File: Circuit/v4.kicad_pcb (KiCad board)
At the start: 2 copper layers, 40 x 49.4 mm, 41 parts, among them J1 Battery, J2 AVR-ISP-6, J3 TX Connector, J4 RX Connector, J5 Alt Battery, J6 Alt RX Conn, J7 Alt TX Conn, J8 Remote temp input 47K @ 25oC, Q1 IRLML6244TRPBF, U1 EL3H7(B)(TA)-VG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

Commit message: Change Opto to HMHA2801
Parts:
- U1: value EL3H7(B)(TA)-VG -> HMHA2801
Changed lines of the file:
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@@
       (effects (font (size 1 1) (thickness 0.15)))
     )
-    (fp_text value "EL3H7(B)(TA)-VG" (at 0.1524 -3.302 180) (layer F.Fab)
+    (fp_text value HMHA2801 (at 0.1524 -3.302 180) (layer F.Fab)
       (effects (font (size 1 1) (thickness 0.15)))
     )

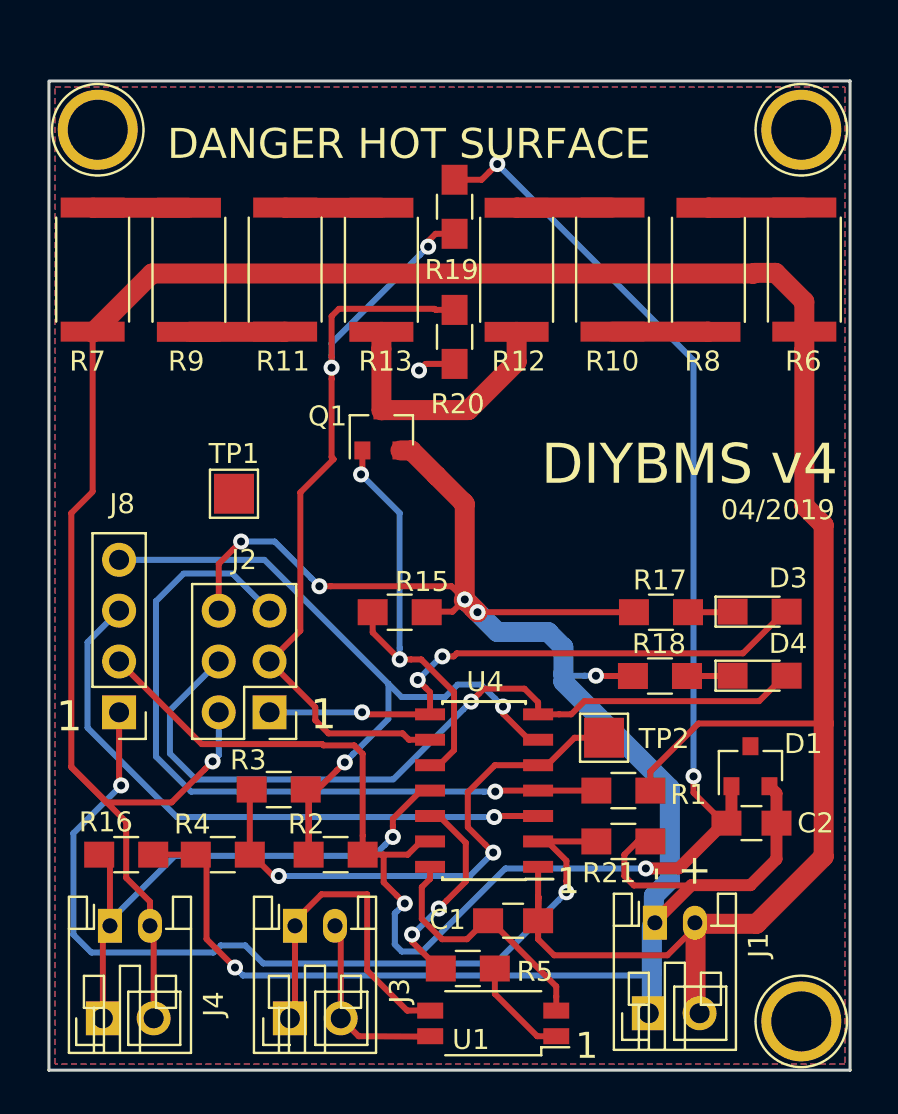
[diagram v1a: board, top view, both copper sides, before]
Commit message: Updated circuit with 510 ohm gate current limit resistor
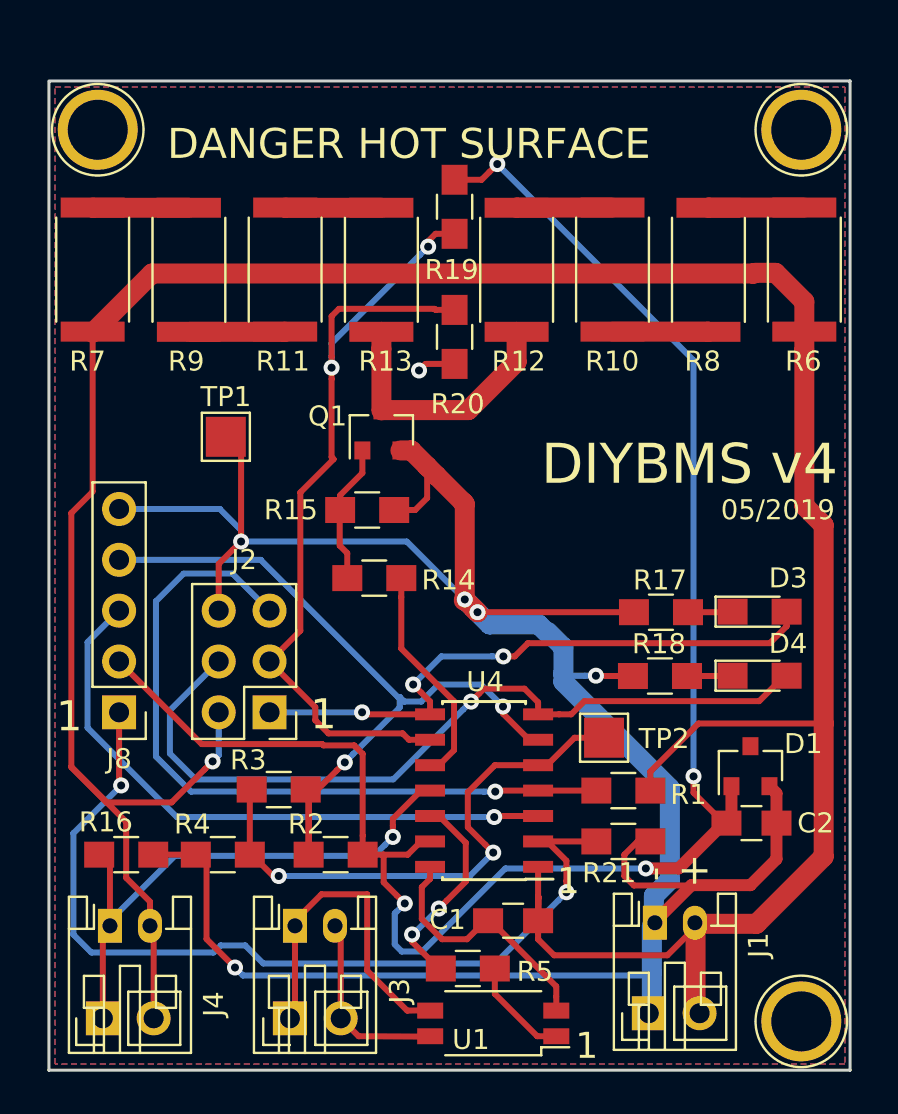
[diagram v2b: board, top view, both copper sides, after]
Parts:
- added R14: 510R, Resistors_SMD:R_0805_HandSoldering, F.Cu at (67.9, 79.7)
- J8: footprint Pin_Headers:Pin_Header_Straight_1x04_Pitch2.54mm -> Pin_Headers:Pin_Header_Straight_1x05_Pitch2.54mm
- R15: value 47K YAGEO RC0805FR-0747KL -> 10K
- moved R15 5.36 mm to (67.5, 76.3)
- moved TP1 2.87 mm to (60.5, 72.6)
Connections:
- Q1 pad 1: DUMP_LOAD_ENABLE -> Net-(Q1-Pad1)
- R15 pad 1: DUMP_LOAD_ENABLE -> Net-(Q1-Pad1)
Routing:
- net GND: track 133.4 -> 147.9 mm, vias 7 -> 6
- net DUMP_LOAD_ENABLE: track 22.0 -> 11.2 mm, vias 2 -> 0
- net Net-(Q1-Pad1): track 0.00 -> 7.01 mm
- net Net-(D3-Pad2): track 29.9 -> 30.5 mm
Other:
- board text added: "05/2019"
- board text removed: "04/2019"

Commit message: Fixes to circuit and tidy up
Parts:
- moved R14 1.37 mm to (67.5, 78.4)
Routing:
- net DUMP_LOAD_ENABLE: track 11.2 -> 13.3 mm
- net ENABLE: track 38.6 -> 40.7 mm
- net Net-(Q1-Pad1): track 7.01 -> 5.55 mm
- net Net-(D3-Pad2): track 30.5 -> 29.4 mm

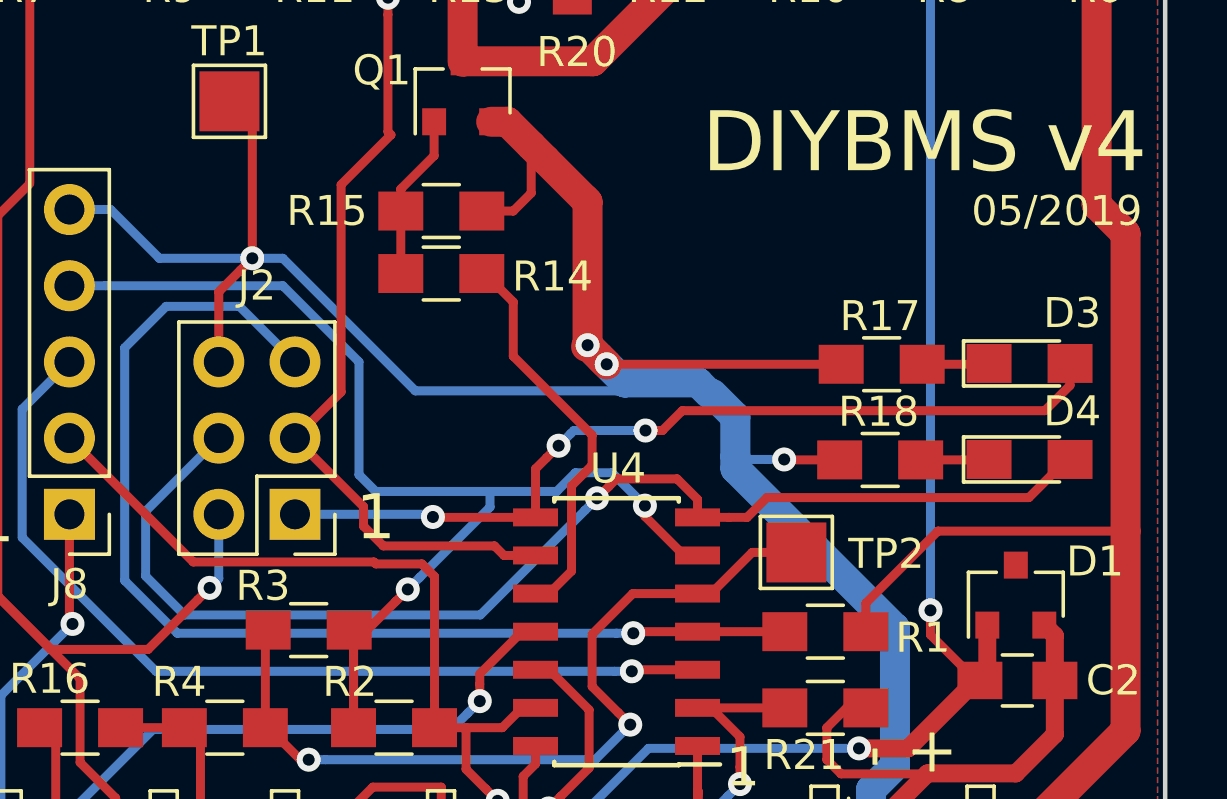
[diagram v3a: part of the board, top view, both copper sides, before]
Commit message: Added 10uF cap to charge MOSFET slower to prevent fast switch on currents resetting MCU
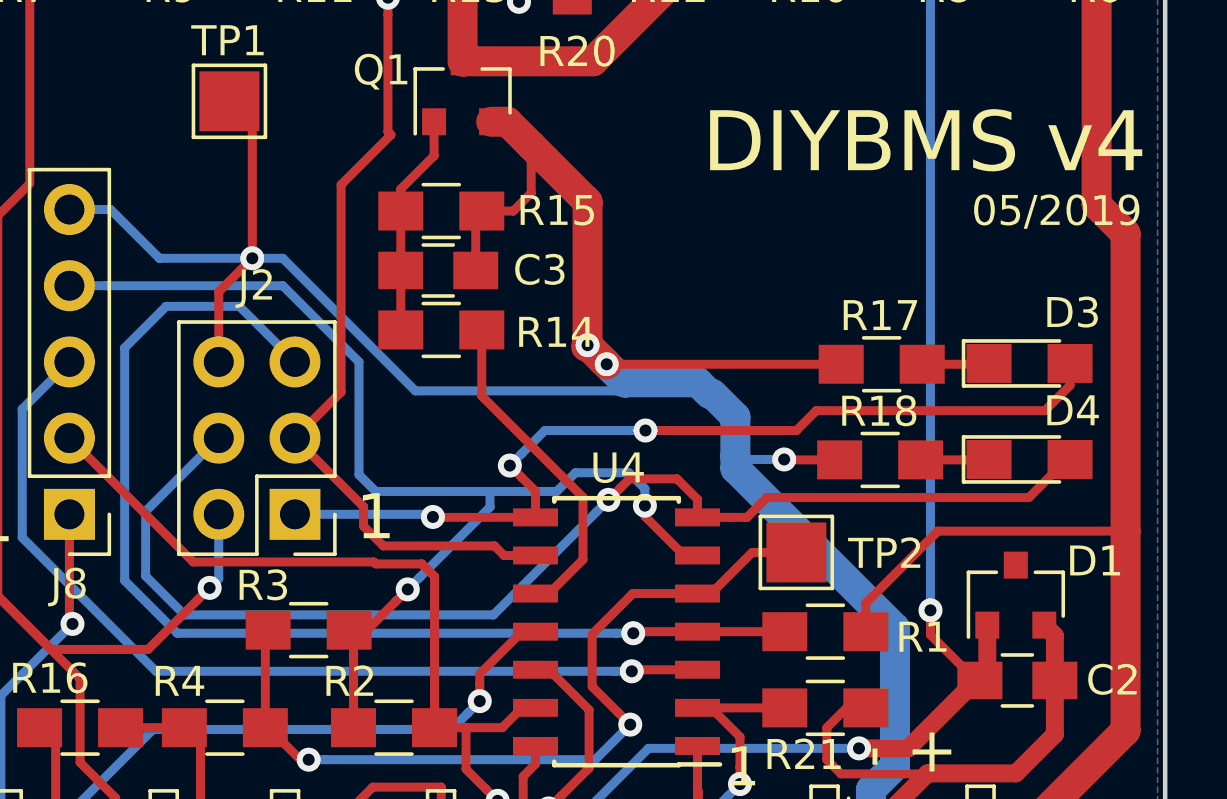
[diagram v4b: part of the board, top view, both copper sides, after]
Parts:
- added C3: 10uF 10V, Capacitors_SMD:C_0805_HandSoldering, F.Cu at (67.4, 78.3)
- R15: value 10K -> 47K
- moved R14 1.88 mm to (67.5, 80.3)
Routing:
- net DUMP_LOAD_ENABLE: track 13.3 -> 11.1 mm
- net GND: track 147.8 -> 149.9 mm
- net Net-(C3-Pad1): track 5.55 -> 7.43 mm
- net Net-(D3-Pad2): track 29.4 -> 30.7 mm
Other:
- board text added: "Calibration value"
- board text added: "github.com/stuartpittaway/diyBMSv4"
- board text removed: "https://github.com/stuartpittaway/diyBMSv4"

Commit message: Updates to circuit design and layout
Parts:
- removed J5: Alt Battery, Pin_Headers:Pin_Header_Straight_1x02_Pitch2.54mm
- removed J6: Alt RX Conn, Pin_Headers:Pin_Header_Straight_1x02_Pitch2.54mm
- removed J7: Alt TX Conn, Pin_Headers:Pin_Header_Straight_1x02_Pitch2.54mm
- removed the REF** at (89.2, 57.3)
- removed the REF** at (54.1, 57.3)
- removed the REF** at (89.2, 101.9)
- removed TP1: TestPoint, TestPoint:TestPoint_Pad_2.0x2.0mm
- added REF**: MountingHole_2.5mm, Mounting_Holes:MountingHole_2.5mm, F.Cu at (54.1, 101.8)
- added REF**: MountingHole_2.5mm, Mounting_Holes:MountingHole_2.5mm, F.Cu at (89.2, 101.8)
- added REF**: MountingHole_2.5mm, Mounting_Holes:MountingHole_2.5mm, F.Cu at (54.1, 57.4)
- added REF**: MountingHole_2.5mm, Mounting_Holes:MountingHole_2.5mm, F.Cu at (89.2, 57.4)
- R10, R12, R8: value 2R2 1W -> 2R2 1W
- moved R20 13.8 mm to (60.5, 75.4), turned to 0 degrees
- moved D4 10.3 mm to (77.3, 81.4)
- moved R19 4.77 mm to (71.3, 65.9)
- moved R18 2.89 mm to (79.5, 83.4), turned to 180 degrees
- moved J3 1.63 mm to (65.5, 97.2)
- moved R3 1.07 mm to (63.1, 91.3)
- moved U1 0.81 mm to (74.6, 101.9)
- moved J1 0.26 mm to (82.1, 96.9)
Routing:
- net GND: track 149.9 -> 120.2 mm
- net VCC: track 155.4 -> 143.7 mm
- net Net-(J2-Pad3): track 44.8 -> 37.7 mm
- net Net-(J3-Pad1): track 17.0 -> 11.6 mm
- net RXD0: track 28.0 -> 22.7 mm
- net Net-(D3-Pad2): track 30.7 -> 34.6 mm
- net 2_VOLT: track 89.4 -> 85.8 mm, vias 4 -> 3
- net Net-(D4-Pad2): track 40.5 -> 37.0 mm
- net Net-(R3-Pad2): track 27.9 -> 24.8 mm
- net ENABLE: track 41.0 -> 37.9 mm
- net Net-(J3-Pad2): track 9.58 -> 7.55 mm
- net Net-(J8-Pad3): track 30.9 -> 29.0 mm
- net Net-(D4-Pad1): track 2.28 -> 3.61 mm
- net TXD0: track 10.4 -> 11.4 mm
- net Net-(Q1-Pad3): track 13.2 -> 12.4 mm
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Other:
- outline, holes or cut-outs redrawn

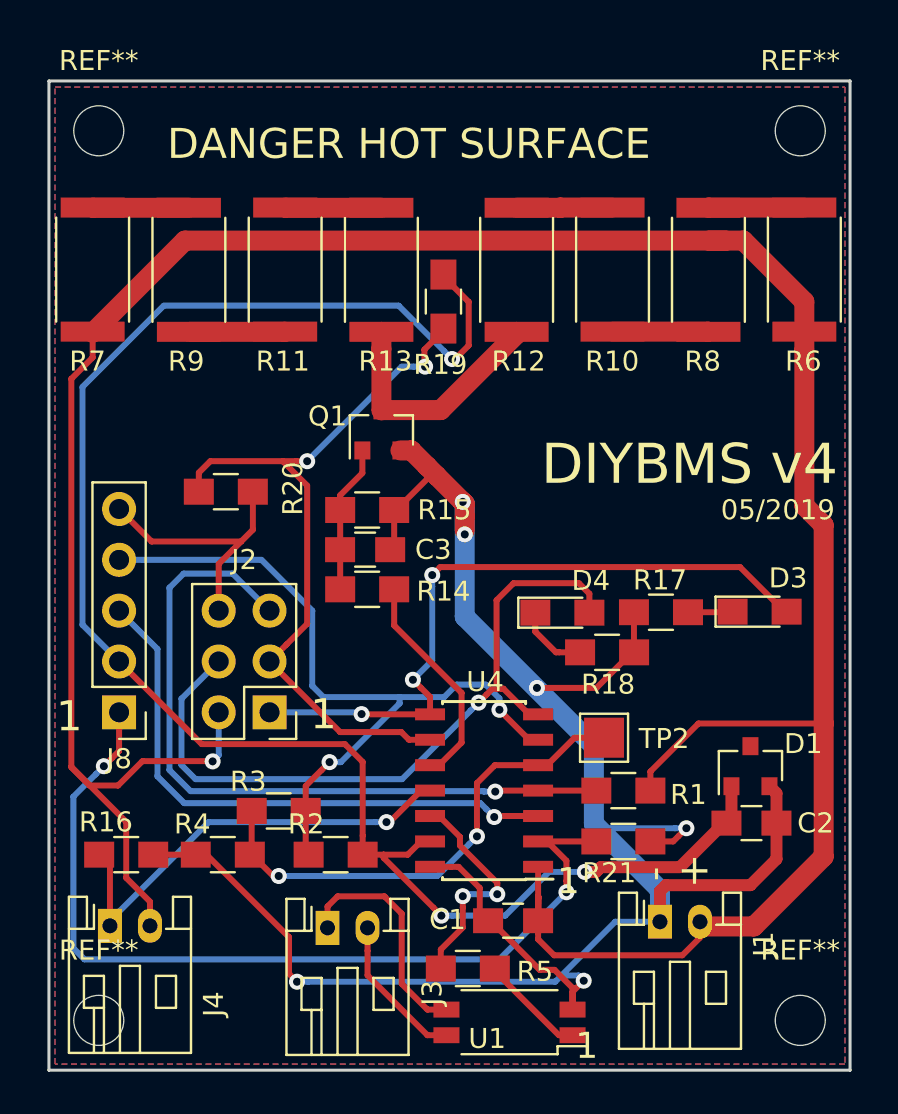
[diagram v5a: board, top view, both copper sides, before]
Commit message: Major tidy up and initial BOM
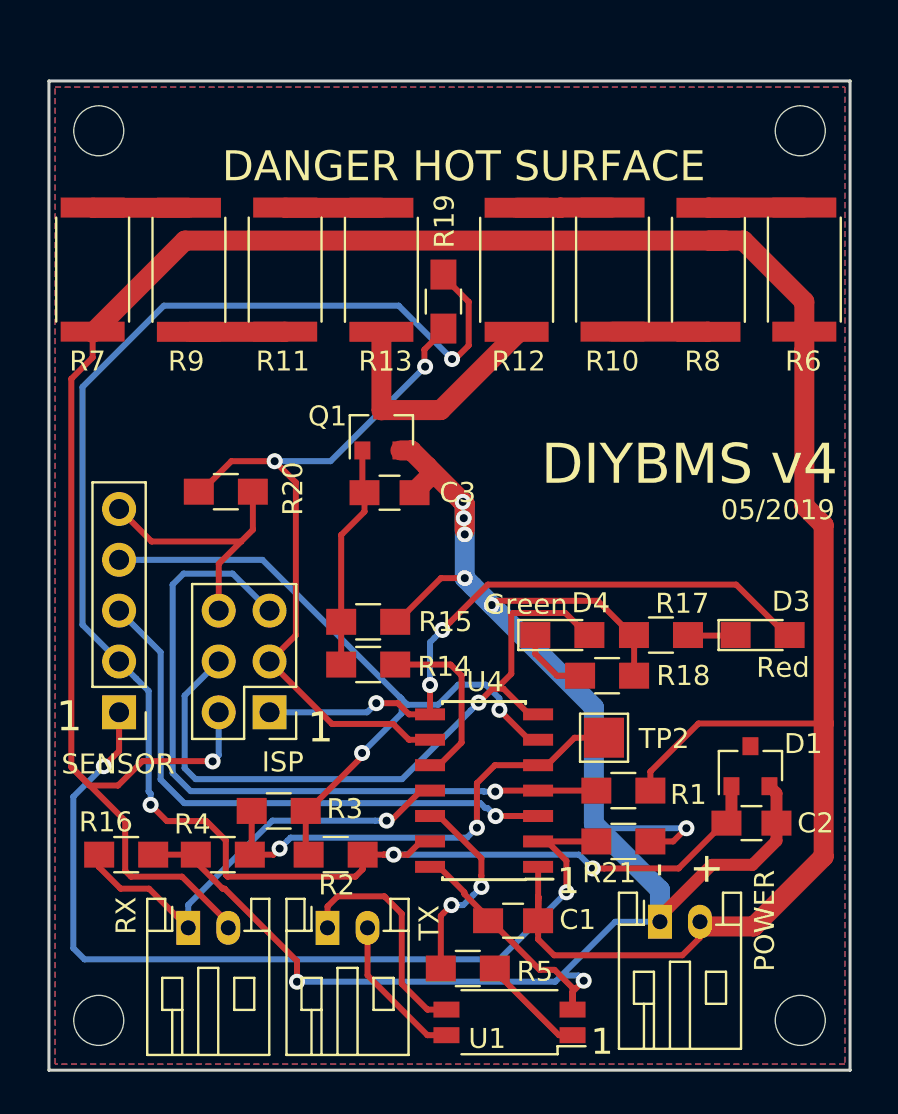
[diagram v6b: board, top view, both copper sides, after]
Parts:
- D3: value RED LED -> Red
- D4: value Green LED -> Green
- moved R15 5.59 mm to (67.6, 81.9)
- moved RX 3.91 mm to (58.6, 97.2)
- moved R14 3.76 mm to (67.6, 84.0)
- moved C3 3.10 mm to (68.6, 75.4)
- moved D3 1.18 mm to (87.3, 82.5)
- moved R18 1.17 mm to (79.5, 84.6)
- moved R17 1.14 mm to (82.2, 82.5)
- moved D4 1.12 mm to (77.3, 82.5)
- renumbered J2 to ISP, J1 to POWER, J4 to RX, J8 to SENSOR, J3 to TX
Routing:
- net Net-(C3-Pad1): track 7.43 -> 11.2 mm
- net VCC: track 143.7 -> 146.9 mm
- net Net-(D3-Pad2): track 34.6 -> 32.1 mm
- net Net-(D4-Pad2): track 37.0 -> 34.7 mm
- net DUMP_LOAD_ENABLE: track 11.1 -> 8.94 mm
- net ENABLE: track 37.9 -> 35.9 mm
- net TXD0: track 11.4 -> 10.1 mm
- net GND: track 120.2 -> 121.4 mm, vias 6 -> 8
- net Net-(R3-Pad2): track 24.8 -> 23.6 mm
- net Net-(J2-Pad3): track 37.7 -> 36.8 mm
- net RXD0: track 22.7 -> 21.9 mm
- net 2_VOLT: track 85.8 -> 86.5 mm, vias 3 -> 4
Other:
- board text added: "MAXIMUM 4.5V BATTERY INPUT 1 AMP DUMP LOAD"
- board text added: "RX"
- board text added: "TX"
- board text removed: "MAXIMUM 5V BATTERY INPUT 1 AMP DUMP LOAD"

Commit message: Added large resistor to board as optional
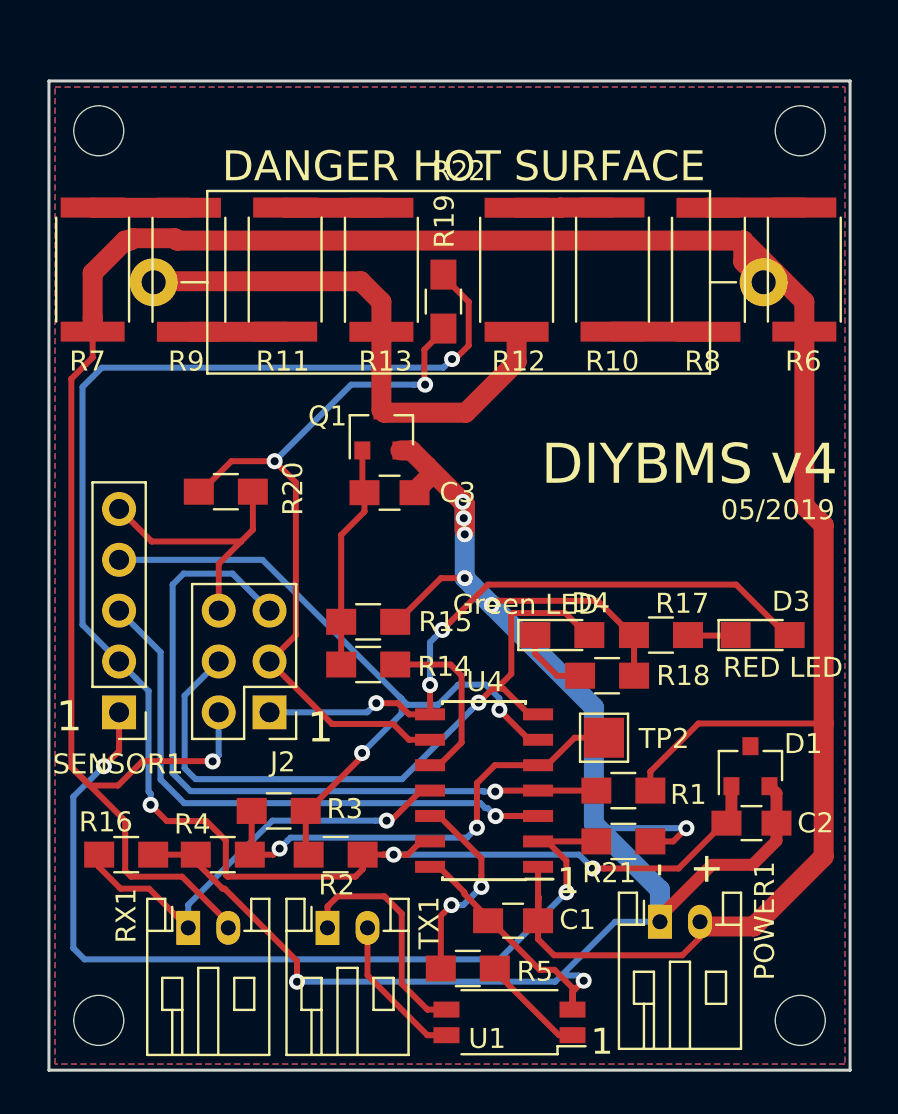
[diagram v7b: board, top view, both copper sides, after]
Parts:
- added R22: 4R4, Resistors_THT:R_Axial_Power_L25.0mm_W9.0mm_P30.48mm, F.Cu at (56.8, 64.9)
- D3: value Red -> RED LED
- D4: value Green -> Green LED
- R19: value Thermistor Sunlord SDNT2012X473F4150FTF -> SDNT2012X473F4150FTF
- renumbered ISP to J2, POWER to POWER1, RX to RX1, SENSOR to SENSOR1, TX to TX1
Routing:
- net Net-(Q1-Pad3): track 12.4 -> 26.6 mm
- net VCC: track 146.9 -> 151.0 mm
- net 2_VOLT: track 86.5 -> 84.3 mm
- net Net-(J2-Pad3): track 36.8 -> 37.4 mm

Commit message: Rounded corners
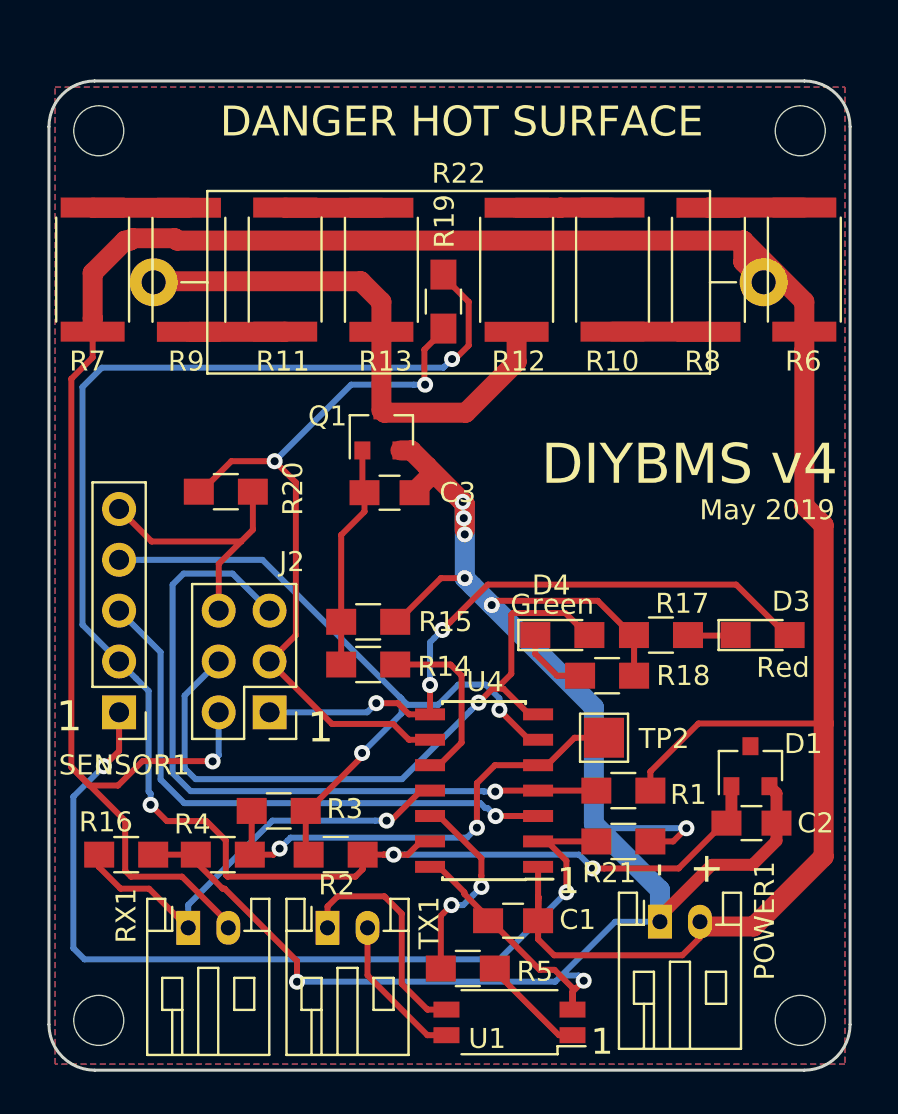
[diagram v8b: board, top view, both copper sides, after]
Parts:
- D3: value RED LED -> Red
- D4: value Green LED -> Green
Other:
- outline, holes or cut-outs redrawn
- board text added: "May 2019"
- board text removed: "05/2019"
